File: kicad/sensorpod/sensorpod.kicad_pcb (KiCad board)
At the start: 2 copper layers, 0 parts

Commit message: Sensor pod footprints all in
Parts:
- added C1: GENERIC_CAPACITOR, 0805, F.Cu at (188.0, 54.6)
- added C10: GENERIC_CAPACITOR, 0805, F.Cu at (166.4, 119.4)
- added C11: GENERIC_CAPACITOR, 0805, F.Cu at (175.3, 114.3)
- added C12: GENERIC_CAPACITOR, 0805, F.Cu at (184.2, 109.2)
- added C13: GENERIC_CAPACITOR, 0805, F.Cu at (179.1, 85.1)
- added C14: GENERIC_CAPACITOR, 0805, F.Cu at (171.4, 80.0)
- added C15: GENERIC_CAPACITOR, 0805, F.Cu at (166.4, 74.9)
- added C16: GENERIC_CAPACITOR, 0805, F.Cu at (30.5, 41.9)
- added C17: GENERIC_CAPACITOR, 0805, F.Cu at (223.5, 74.9)
- added C18: GENERIC_CAPACITOR, 0805, F.Cu at (217.2, 80.0)
- added C19: GENERIC_CAPACITOR, 0805, F.Cu at (128.3, 39.4)
- added C2: GENERIC_CAPACITOR, 0805, F.Cu at (188.0, 64.8)
- added C20: GENERIC_CAPACITOR, 0805, F.Cu at (209.6, 86.4)
- added C21: GENERIC_CAPACITOR, 0805, F.Cu at (193.0, 130.8)
- added C22: GENERIC_CAPACITOR, 0805, F.Cu at (191.8, 123.2)
- added C23: GENERIC_CAPACITOR, 0805, F.Cu at (193.0, 118.1)
- added C24: GENERIC_CAPACITOR, 0805, F.Cu at (193.0, 113.0)
- added C25: GENERIC_CAPACITOR, 0805, F.Cu at (193.0, 22.9)
- added C26: GENERIC_CAPACITOR, 0805, F.Cu at (26.7, 49.5)
- added C27: GENERIC_CAPACITOR, 0805, F.Cu at (82.5, 22.9)
- added C28: GENERIC_CAPACITOR, 0805, F.Cu at (30.5, 21.6)
- added C29: GENERIC_CAPACITOR, 0805, F.Cu at (45.7, 67.3)
- added C3: GENERIC_CAPACITOR, 0805, F.Cu at (188.0, 74.9)
- added C30: GENERIC_CAPACITOR, 0805, F.Cu at (73.7, 55.9)
- added C31: GENERIC_CAPACITOR, 0805, F.Cu at (59.7, 43.2)
- added C32: GENERIC_CAPACITOR, 0805, F.Cu at (72.4, 21.6)
- added C33: GENERIC_CAPACITOR, 0805, F.Cu at (106.7, 33.0)
- added C4: GENERIC_CAPACITOR, 0805, F.Cu at (188.0, 85.1)
- added C5: GENERIC_CAPACITOR, 0805, F.Cu at (201.9, 109.2)
- added C6: GENERIC_CAPACITOR, 0805, F.Cu at (210.8, 114.3)
- added C7: GENERIC_CAPACITOR, 0805, F.Cu at (219.7, 119.4)
- added C8: GENERIC_CAPACITOR, 0805, F.Cu at (228.6, 124.5)
- added C9: GENERIC_CAPACITOR, 0805, F.Cu at (157.5, 124.5)
- added D1: GENERIC_DIODE, SOD-323, F.Cu at (193.0, 20.3)
- added IR1: TSOP38438, Minicast, F.Cu at (257.8, 199.4)
- added IR2: TSOP38438, Minicast, F.Cu at (240.0, 198.1)
- added IR3: TSOP38438, Minicast, F.Cu at (218.4, 200.7)
- added IR4: TSOP38438, Minicast, F.Cu at (190.5, 198.1)
- added IR5: TSOP38438, Minicast, F.Cu at (176.5, 196.8)
- added IR6: TSOP38438, Minicast, F.Cu at (158.8, 196.8)
- added IR7: TSOP38438, Minicast, F.Cu at (143.5, 196.8)
- added M1: MOTOR, Header_2x1, F.Cu at (193.0, 26.7)
- added NP1: WS2812B, 5050, F.Cu at (193.0, 54.6)
- added NP10: WS2812B, 5050, F.Cu at (163.8, 114.3)
- added NP11: WS2812B, 5050, F.Cu at (172.7, 109.2)
- added NP12: WS2812B, 5050, F.Cu at (181.6, 104.1)
- added NP13, NP20, NP21, NP22, NP23, NP24: WS2812B, 5050, F.Cu at (59.7, 43.2)
- added NP14: WS2812B, 5050, F.Cu at (148.6, 73.7)
- added NP15: WS2812B, 5050, F.Cu at (170.2, 68.6)
- added NP16: WS2812B, 5050, F.Cu at (160.0, 61.0)
- added NP17: WS2812B, 5050, F.Cu at (232.4, 69.8)
- added NP18: WS2812B, 5050, F.Cu at (223.5, 87.6)
- added NP19: WS2812B, 5050, F.Cu at (232.4, 82.5)
- added NP2: WS2812B, 5050, F.Cu at (193.0, 64.8)
- added NP3: WS2812B, 5050, F.Cu at (193.0, 74.9)
- added NP4: WS2812B, 5050, F.Cu at (193.0, 85.1)
- added NP5: WS2812B, 5050, F.Cu at (204.5, 104.1)
- added NP6: WS2812B, 5050, F.Cu at (213.4, 109.2)
- added NP7: WS2812B, 5050, F.Cu at (222.2, 114.3)
- added NP8: WS2812B, 5050, F.Cu at (231.1, 119.4)
- added NP9: WS2812B, 5050, F.Cu at (154.9, 119.4)
- added P1: HEADER_(8_WAY), Header_4x2, F.Cu at (193.0, 41.9)
- added Q1: IRFML8244TRPBF, SOT-23, F.Cu at (193.0, 34.3)
- added R1: GENERIC_RESISTOR, 0805, F.Cu at (92.7, 20.3)
- added R10: GENERIC_RESISTOR, 0805, F.Cu at (101.6, 26.7)
- added R11: GENERIC_RESISTOR, 0805, F.Cu at (17.8, 74.9)
- added R12: GENERIC_RESISTOR, 0805, F.Cu at (61.0, 54.6)
- added R13, R6: GENERIC_RESISTOR, 0805, F.Cu at (59.7, 43.2)
- added R14: GENERIC_RESISTOR, 0805, F.Cu at (64.8, 31.8)
- added R15: GENERIC_RESISTOR, 0805, F.Cu at (53.3, 38.1)
- added R16: GENERIC_RESISTOR, 0805, F.Cu at (45.7, 19.1)
- added R2: GENERIC_RESISTOR, 0805, F.Cu at (27.9, 73.7)
- added R3: GENERIC_RESISTOR, 0805, F.Cu at (109.2, 21.6)
- added R4: GENERIC_RESISTOR, 0805, F.Cu at (87.6, 99.1)
- added R5: GENERIC_RESISTOR, 0805, F.Cu at (62.2, 68.6)
- added R7: GENERIC_RESISTOR, 0805, F.Cu at (74.9, 41.9)
- added R8: GENERIC_RESISTOR, 0805, F.Cu at (20.3, 59.7)
- added R9: GENERIC_RESISTOR, 0805, F.Cu at (72.4, 35.6)
- added SR1: SN74HC165, SOIC-16, F.Cu at (190.5, 175.3)

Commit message: Initial sensor pod PCB
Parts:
- moved R2 208.9 mm to (236.2, 90.2), turned to 90 degrees
- moved C28 206.1 mm to (221.0, 100.3)
- moved R11 201.8 mm to (213.4, 124.5), turned to 270 degrees
- moved C29 181.9 mm to (218.4, 124.5), turned to 270 degrees
- moved R16 174.8 mm to (217.2, 53.3), turned to 180 degrees
- moved NP24 165.4 mm to (193.0, 141.0), turned to 90 degrees
- moved R5 161.9 mm to (207.0, 141.0)
- moved R9 160.1 mm to (221.0, 95.2)
- moved NP23 159.6 mm to (193.0, 130.8), turned to 90 degrees
- moved R12 158.5 mm to (203.2, 124.5), turned to 270 degrees
- moved C26 156.6 mm to (182.9, 61.0), turned to 270 degrees
- moved NP22 154.2 mm to (193.0, 120.7), turned to 90 degrees
- moved C27 153.9 mm to (221.0, 90.2)
- moved R3 152.9 mm to (236.2, 106.7), turned to 90 degrees
- moved NP20 152.6 mm to (204.5, 91.4), turned to 30 degrees
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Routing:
- net N-0000044: track 0.00 -> 19.6 mm
- net N-0000021: track 0.00 -> 11.7 mm
- net N-0000036: track 0.00 -> 6.73 mm
- net N-000007: track 0.00 -> 6.73 mm
- net N-000006: track 0.00 -> 6.73 mm
- net N-0000046: track 0.00 -> 6.73 mm
- net N-0000035: track 0.00 -> 6.73 mm
- net N-0000014: track 0.00 -> 6.73 mm
- net N-0000016: track 0.00 -> 6.63 mm
- net N-0000015: track 0.00 -> 6.63 mm
- net N-0000043: track 0.00 -> 6.63 mm
- net N-0000042: track 0.00 -> 6.63 mm
- net N-0000013: track 0.00 -> 6.63 mm
- net N-0000040: track 0.00 -> 6.63 mm
- net N-0000045: track 0.00 -> 6.39 mm
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
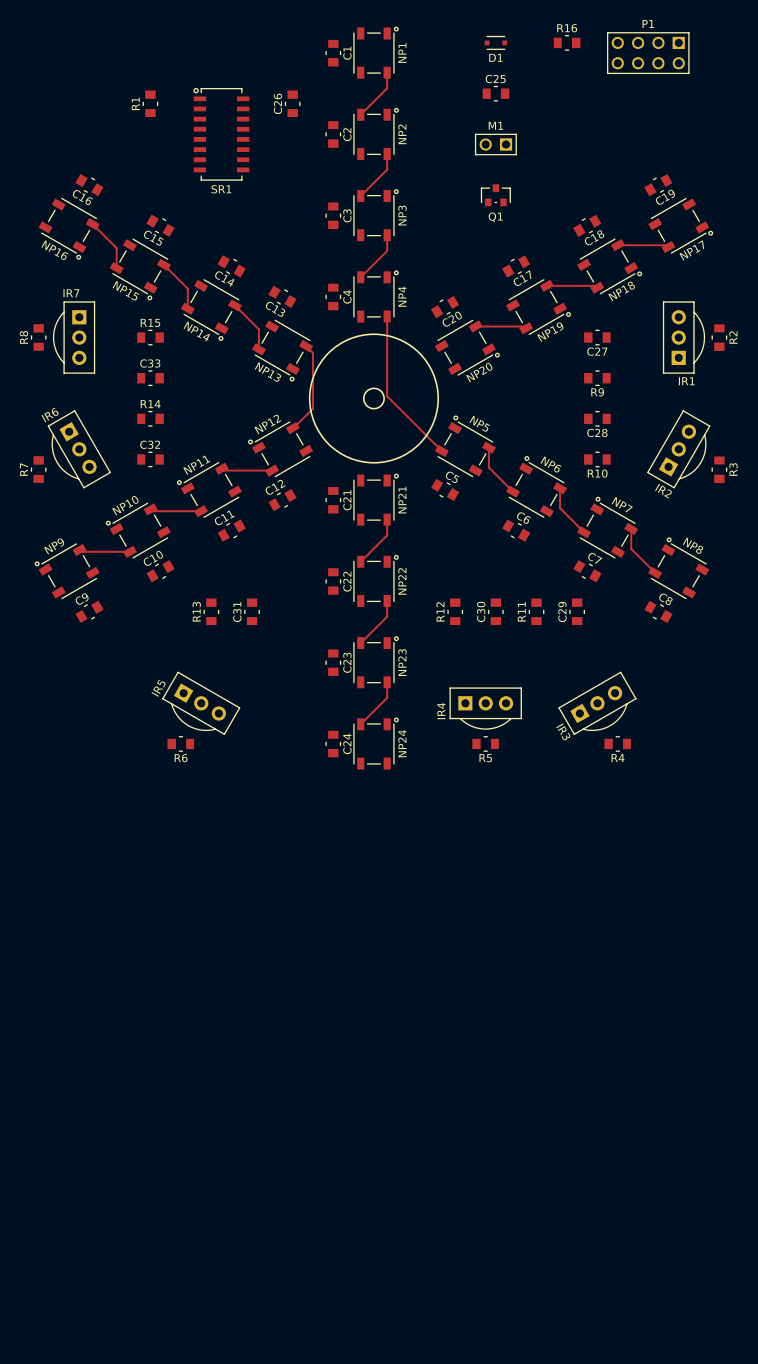
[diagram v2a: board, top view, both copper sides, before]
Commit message: Reduced component count so it will fit
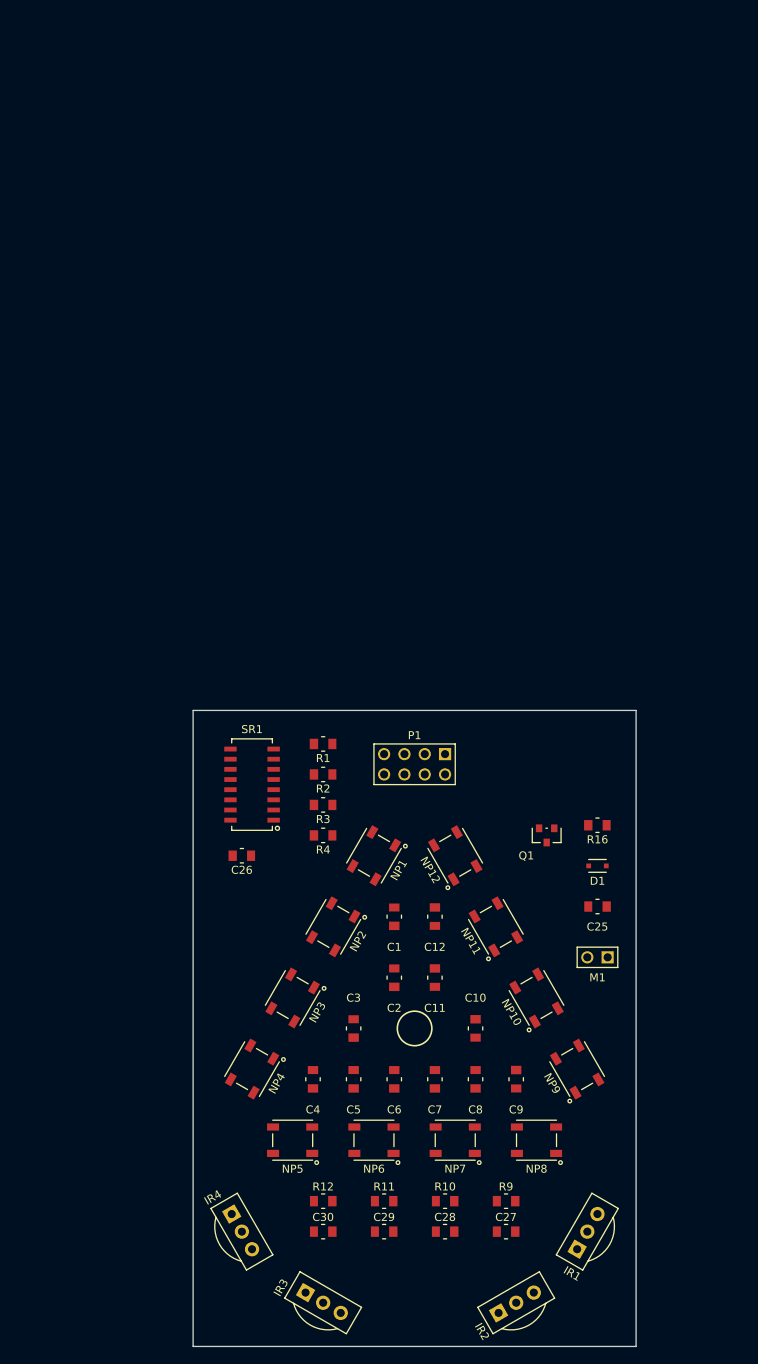
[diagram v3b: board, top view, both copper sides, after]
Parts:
- removed C13, C14, C15, C16, C17, C18, C19, C20, C21, C22, C23, C24, C31, C32, C33: GENERIC_CAPACITOR, 0805
- removed IR5, IR6, IR7: TSOP38438, Minicast
- removed NP13, NP14, NP15, NP16, NP17, NP18, NP19, NP20, NP21, NP22, NP23, NP24: WS2812B, 5050
- removed R13, R14, R15, R5, R6, R7, R8: GENERIC_RESISTOR, 0805
- moved C27 112.3 mm to (209.6, 201.9), turned to 180 degrees
- moved IR1 112.3 mm to (219.7, 201.9), turned to 330 degrees
- moved IR2 108.6 mm to (210.8, 210.8), turned to 300 degrees
- moved C1 108.2 mm to (195.6, 162.6)
- moved C2 105.7 mm to (195.6, 170.2)
- moved D1 103.7 mm to (221.0, 156.2)
- moved R9 103.5 mm to (209.6, 198.1), turned to 180 degrees
- moved C28 103.4 mm to (201.9, 201.9), turned to 180 degrees
- moved C25 102.4 mm to (221.0, 161.3)
- moved M1 102.4 mm to (221.0, 167.6)
- moved C3 101.6 mm to (190.5, 176.5)
- moved NP1 100.3 mm to (193.0, 154.9), turned to 60 degrees
- moved NP2 99.2 mm to (188.0, 163.8), turned to 60 degrees
- moved NP3 98.3 mm to (182.9, 172.7), turned to 60 degrees
- moved R16 97.9 mm to (221.0, 151.1), turned to 0 degrees
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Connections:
- IR1 pad 1: N-0000019 (its old number) -> N-000009
- IR2 pad 1: N-0000031 (its old number) -> N-000008
- IR3 pad 1: N-0000034 -> N-000007
- NP12 pad 2: N-0000021 (its old number) -> (no net)
- R2 pad 1: N-0000019 (its old number) -> N-0000014
- R3 pad 1: N-0000031 (its old number) -> N-0000013
- R4 pad 1: N-0000034 -> N-0000012
- SR1 pad 12: N-0000034 -> N-000007
- SR1 pad 13: N-0000031 (its old number) -> N-000008
- SR1 pad 14: N-0000019 (its old number) -> N-000009
- SR1 pad 3: N-000002 (its old number) -> N-0000012
- SR1 pad 4: N-0000017 (its old number) -> N-0000013
- SR1 pad 5: N-0000029 (its old number) -> N-0000014
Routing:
- net N-0000024: track 19.6 -> 0.00 mm
- net N-0000021 (its old number): track 11.7 -> 0.00 mm
- net N-0000031: track 6.73 -> 0.00 mm
- net N-000007: track 6.73 -> 0.00 mm
- net N-000006 (its old number): track 6.73 -> 0.00 mm
- net N-0000033: track 6.73 -> 0.00 mm
- net N-0000032: track 6.73 -> 0.00 mm
- net N-0000014: track 6.73 -> 0.00 mm
- net N-0000016: track 6.63 -> 0.00 mm
- net N-0000015 (its old number): track 6.63 -> 0.00 mm
- net N-0000026: track 6.63 -> 0.00 mm
- net N-0000025: track 6.63 -> 0.00 mm
- net N-0000013: track 6.63 -> 0.00 mm
- net N-0000027: track 6.63 -> 0.00 mm
- net N-0000029: track 6.39 -> 0.00 mm
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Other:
- board outline added: 55.4 x 79.5 mm

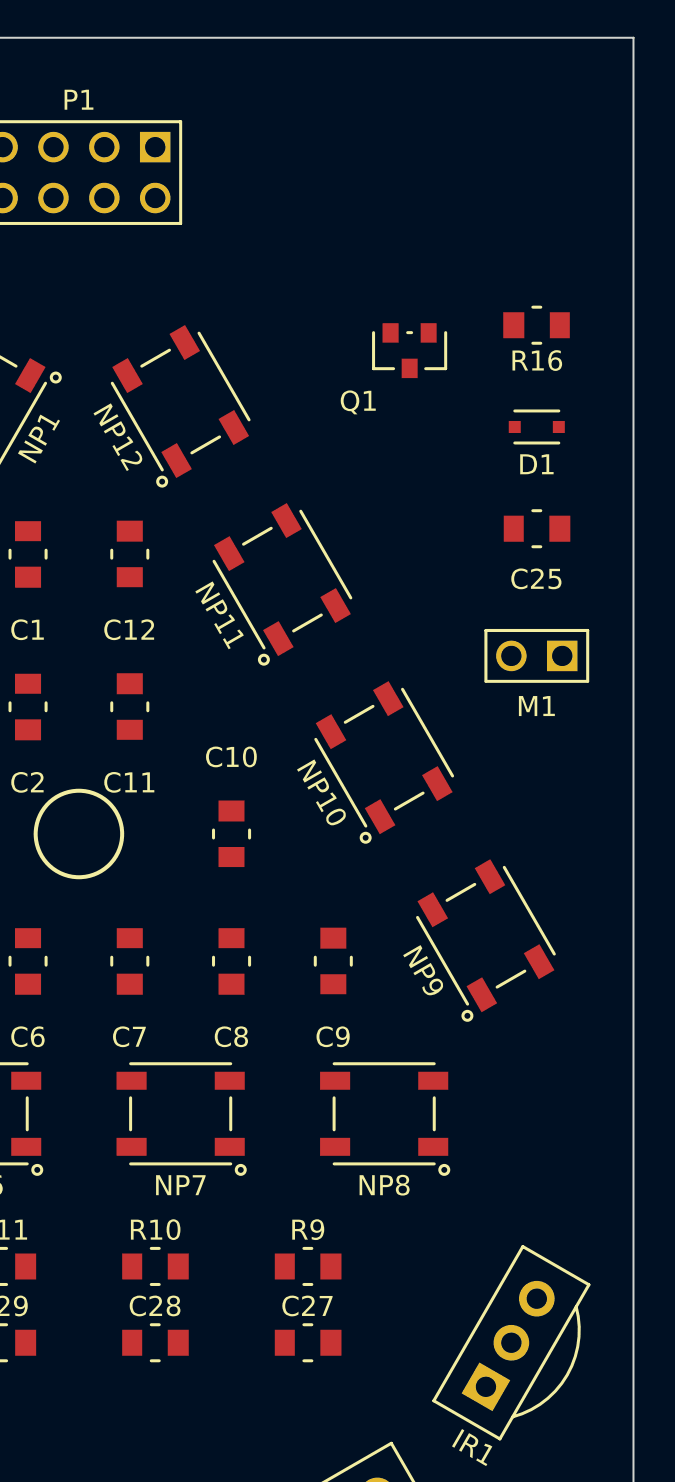
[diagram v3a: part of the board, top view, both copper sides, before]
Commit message: Swap a few cable pins
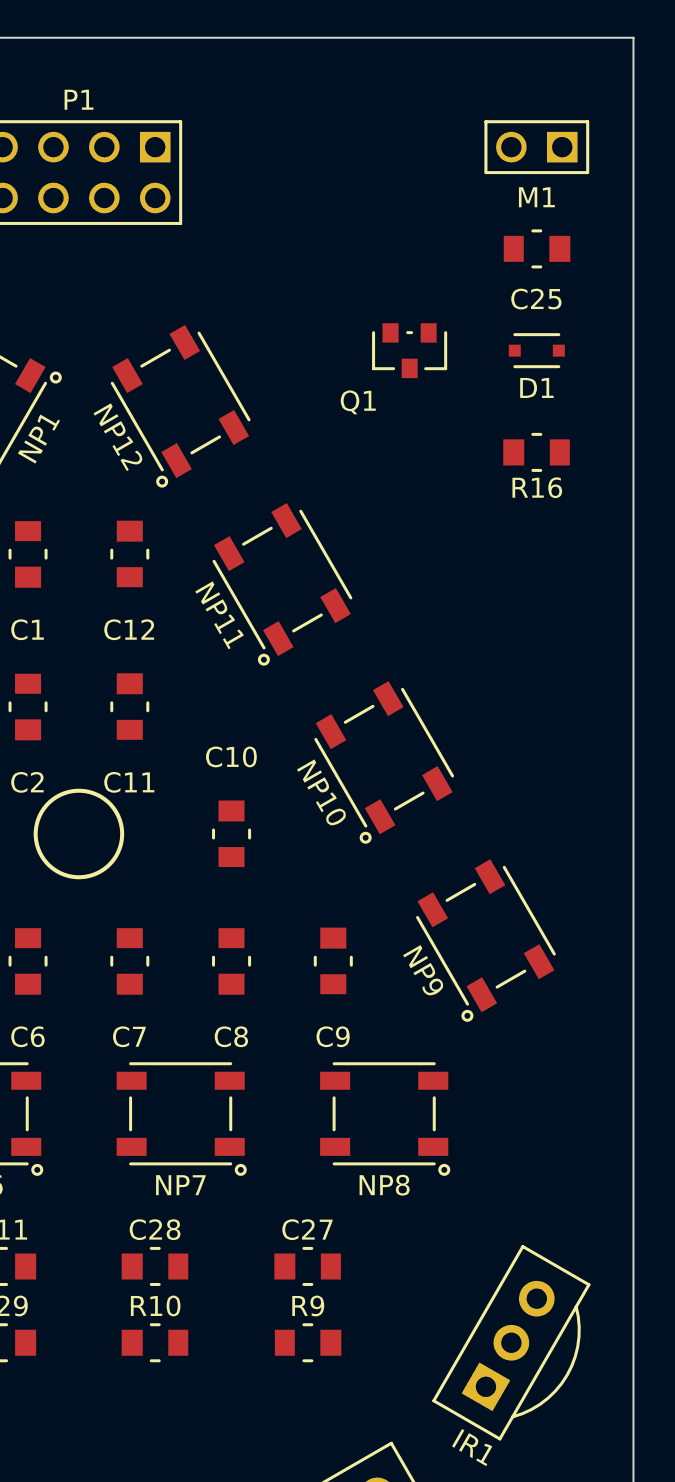
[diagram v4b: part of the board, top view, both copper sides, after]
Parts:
- moved M1 25.4 mm to (221.0, 142.2)
- moved C25 14.0 mm to (221.0, 147.3)
- moved R16 6.35 mm to (221.0, 157.5)
- moved C27 3.81 mm to (209.6, 198.1), turned to 0 degrees
- moved C28 3.81 mm to (201.9, 198.1), turned to 0 degrees
- moved D1 3.81 mm to (221.0, 152.4)
- moved R10 3.81 mm to (201.9, 201.9), turned to 0 degrees
- moved R9 3.81 mm to (209.6, 201.9)
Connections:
- NP1 pad 4: N-0000018 (its old number) -> N-0000019
- P1 pad 1: +5V -> N-0000020
- P1 pad 2: N-0000018 (its old number) -> +5V
- P1 pad 3: N-0000011 (its old number) -> GND
- P1 pad 4: GND -> N-0000019
- Q1 pad 1: N-0000011 (its old number) -> N-0000020

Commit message: Prototype sensor pod PCB complete
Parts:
- moved C26 1.91 mm to (178.4, 154.9)
- moved SR1 1.91 mm to (179.7, 146.1)
- turned C7 to 270 degrees
- turned C8 to 270 degrees
- turned NP5 to 180 degrees
- turned NP6 to 180 degrees
- turned NP7 to 180 degrees
- turned NP8 to 180 degrees
- turned R9 to 0 degrees
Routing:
- net +5V: track 0.00 -> 408.0 mm, vias 0 -> 4
- net GND: track 0.00 -> 198.4 mm, vias 0 -> 17
- net N-0000010: track 0.00 -> 93.8 mm, vias 0 -> 2
- net N-000009: track 0.00 -> 91.1 mm, vias 0 -> 2
- net N-000008: track 0.00 -> 73.5 mm, vias 0 -> 2
- net N-000007: track 0.00 -> 63.3 mm, vias 0 -> 2
- net N-0000017: track 0.00 -> 26.8 mm, vias 0 -> 2
- net N-0000022: track 0.00 -> 26.2 mm
- net N-0000018: track 0.00 -> 20.9 mm, vias 0 -> 2
- net N-0000015: track 0.00 -> 20.8 mm
- net N-0000020: track 0.00 -> 17.5 mm
- net N-000001: track 0.00 -> 16.2 mm
- net N-0000016: track 0.00 -> 15.3 mm
- net N-000004: track 0.00 -> 12.9 mm
- net N-000003: track 0.00 -> 10.6 mm
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- added copper zone on B.Cu, net GND
